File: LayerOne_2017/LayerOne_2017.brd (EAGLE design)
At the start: 73.6 x 73.7 mm, 71 parts, among them IC1 STM32F446_LQFP64LQFP64, IC2 REG1117, J1 SPI_TFT_DISPLAY, Q1 2N2222, Q2 MMBT2222A, U1 SN65HVD235DR, U2 SN65HVD235DR, U4 SDCARD, U5 FERRITE0805, X1 STEREOJACK, X2 MINI-USB-32005-301

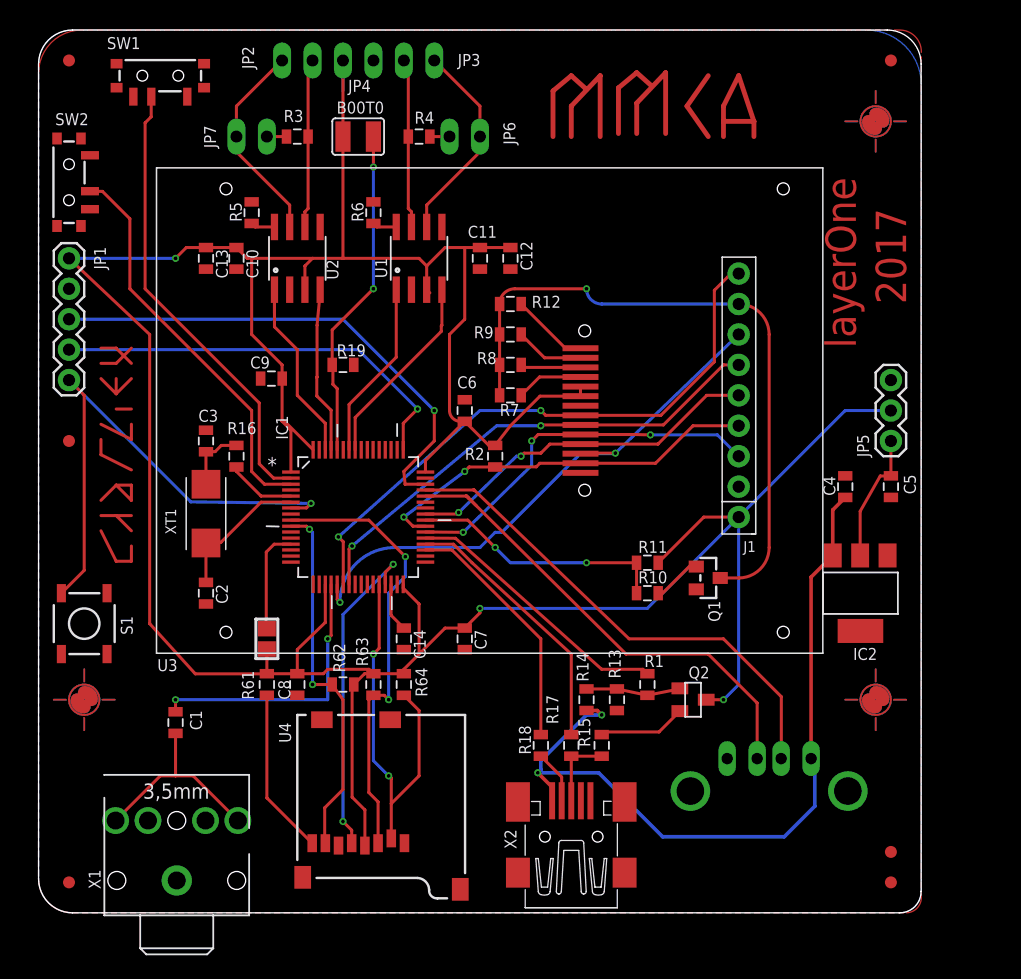
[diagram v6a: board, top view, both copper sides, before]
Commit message: updates to smaller lqfp64 board.
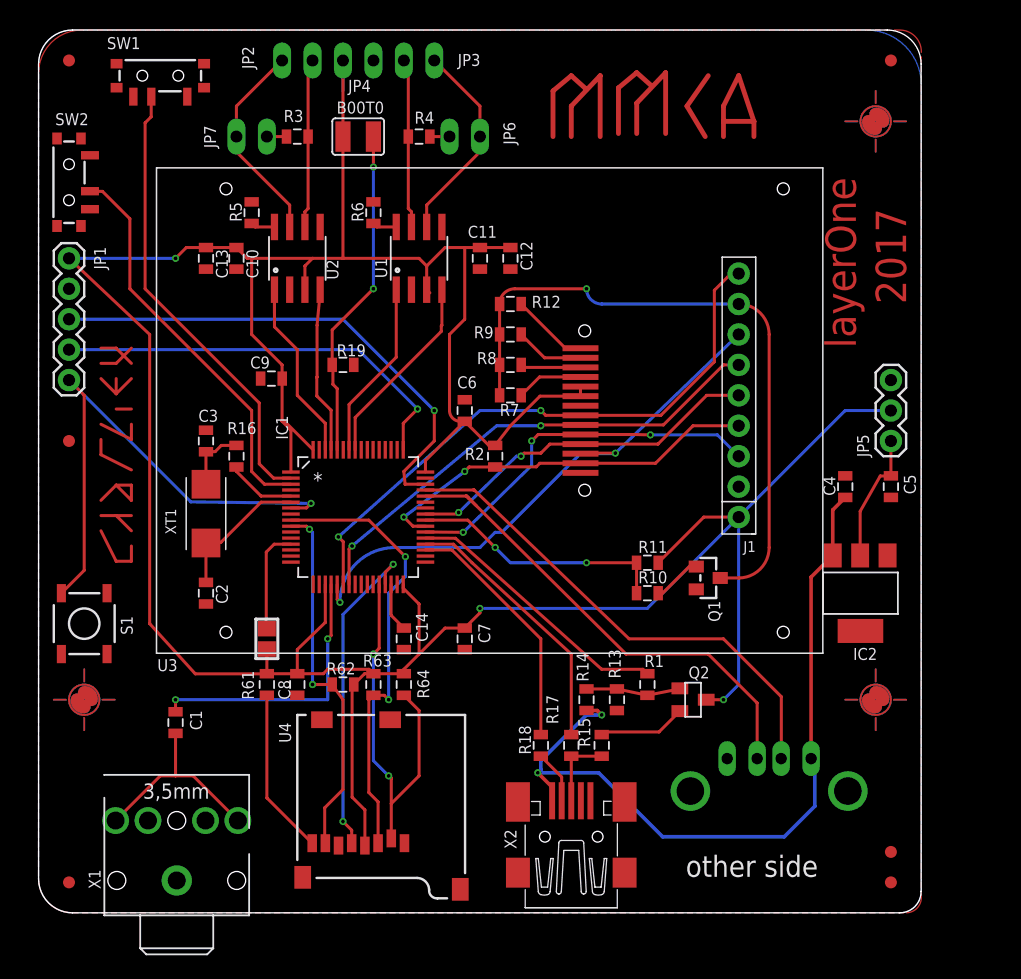
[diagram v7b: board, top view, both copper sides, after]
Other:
- board text added: "other side"
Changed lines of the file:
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@@
 <setting verticaltext="up"/>
 </settings>
-<grid distance="0.05" unitdist="inch" unit="mm" style="lines" multiple="1" display="yes" altdistance="0.001" altunitdist="inch" altunit="inch"/>
+<grid distance="0.05" unitdist="inch" unit="inch" style="lines" multiple="1" display="yes" altdistance="0.005" altunitdist="inch" altunit="inch"/>
 <layers>
 <layer number="1" name="Top" color="4" fill="1" visible="yes" active="yes"/>
@@
 <layer number="14" name="Route14" color="1" fill="6" visible="no" active="no"/>
 <layer number="15" name="Route15" color="4" fill="6" visible="no" active="no"/>
-<layer number="16" name="Bottom" color="1" fill="1" visible="no" active="yes"/>
+<layer number="16" name="Bottom" color="1" fill="1" visible="yes" active="yes"/>
 <layer number="17" name="Pads" color="2" fill="1" visible="yes" active="yes"/>
 <layer number="18" name="Vias" color="2" fill="1" visible="yes" active="yes"/>
@@
 <layer number="49" name="Reference" color="7" fill="1" visible="no" active="yes"/>
 <layer number="50" name="dxf" color="7" fill="1" visible="no" active="no"/>
-<layer number="51" name="tDocu" color="7" fill="1" visible="yes" active="yes"/>
+<layer number="51" name="tDocu" color="7" fill="1" visible="no" active="yes"/>
 <layer number="52" name="bDocu" color="7" fill="1" visible="no" active="yes"/>
 <layer number="53" name="tGND_GNDA" color="7" fill="9" visible="no" active="no"/>
@@
 <layer number="119" name="KAP_TEKEN" color="7" fill="1" visible="no" active="yes"/>
 <layer number="120" name="120" color="7" fill="1" visible="no" active="yes"/>
-<layer number="121" name="_tsilk" color="7" fill="1" visible="no" active="yes"/>
+<layer number="121" name="_tsilk" color="7" fill="1" visible="yes" active="yes"/>
 <layer number="122" name="_bsilk" color="7" fill="1" visible="no" active="yes"/>
 <layer number="123" name="tTestmark" color="7" fill="1" visible="no" active="yes"/>
@@
 <text x="68.199" y="47.117" size="2.54" layer="1" font="vector" rot="R90">layerOne</text>
 <text x="72.39" y="50.8" size="2.54" layer="1" font="vector" rot="R90">2017</text>
+<text x="54" y="3" size="1.778" layer="121">other side</text>
 </plain>
 <attributes>
@@
 <attribute name="DIGIKEY" value="RMCF0603JT10K0CT-ND" x="-87.63" y="100.33" size="1.778" layer="27" display="off"/>
 <attribute name="OC_NEWARK" value="unknown" x="-87.63" y="100.33" size="1.778" layer="27" display="off"/>
-<attribute name="NAME" x="25.5905" y="20.066" size="1" layer="25" ratio="10" rot="R90"/>
+<attribute name="NAME" x="26.4414" y="20.8915" size="1" layer="25" ratio="10" rot="R180"/>
 <attribute name="VALUE" x="24.384" y="17.653" size="0.4064" layer="27"/>
 </element>
@@
 <attribute name="DIGIKEY" value="RMCF0603JT10K0CT-ND" x="-60.96" y="-12.7" size="1.778" layer="27" rot="R90" display="off"/>
 <attribute name="OC_NEWARK" value="unknown" x="-60.96" y="-12.7" size="1.778" layer="27" rot="R90" display="off"/>
-<attribute name="NAME" x="27.4955" y="20.574" size="1" layer="25" ratio="10" rot="R90"/>
+<attribute name="NAME" x="29.4894" y="21.5519" size="1" layer="25" ratio="10" rot="R180"/>
 <attribute name="VALUE" x="29.337" y="18.034" size="0.4064" layer="27" rot="R90"/>
 </element>
@@
 <attribute name="DIGIKEY" value="RMCF0603JT10K0CT-ND" x="-58.42" y="-22.86" size="1.778" layer="27" rot="R90" display="off"/>
 <attribute name="OC_NEWARK" value="unknown" x="-58.42" y="-22.86" size="1.778" layer="27" rot="R90" display="off"/>
-<attribute name="NAME" x="32.4485" y="18.034" size="1" layer="25" ratio="10" rot="R90"/>
+<attribute name="NAME" x="32.6009" y="17.8816" size="1" layer="25" ratio="10" rot="R90"/>
 <attribute name="VALUE" x="31.877" y="18.034" size="0.4064" layer="27" rot="R90"/>
 </element>
@@
 </element>
 <element name="C7" library="SparkFun-Passives" package="0805" value="100nF" x="35.56" y="22.86" smashed="yes" rot="R270">
-<attribute name="NAME" x="36.3855" y="23.622" size="1" layer="25" ratio="10" rot="R270"/>
+<attribute name="NAME" x="36.6903" y="24.1554" size="1" layer="25" ratio="10" rot="R270"/>
 <attribute name="VALUE" x="34.163" y="23.876" size="0.4064" layer="27" rot="R270"/>
 </element>
@@
 </element>
 <element name="C14" library="SparkFun-Passives" package="0805" value="4.7uF/X7R" x="30.48" y="22.86" smashed="yes" rot="R270">
-<attribute name="NAME" x="31.3055" y="23.622" size="1" layer="25" ratio="10" rot="R270"/>
+<attribute name="NAME" x="31.4833" y="25.0444" size="1" layer="25" ratio="10" rot="R270"/>
 <attribute name="VALUE" x="29.083" y="23.876" size="0.4064" layer="27" rot="R270"/>
 </element>
@@
 <vertex x="71.86395" y="0" curve="90"/>
 </polygon>
-<polygon width="0.4064" layer="1" isolate="0.3" orphans="yes">
+<polygon width="0.4064" layer="1" isolate="0.34" orphans="yes">
 <vertex x="73.66" y="1.27"/>
 <vertex x="73.66" y="71.86395" curve="90"/>
@@
 <contactref element="SW2" pad="C"/>
 <contactref element="S1" pad="1"/>
-<wire x1="67.31" y1="36.46" x2="71.12" y2="34.66" width="0" layer="19" extent="1-1"/>
-<wire x1="70.8406" y1="29.8196" x2="71.12" y2="34.66" width="0" layer="19" extent="1-1"/>
-<wire x1="58.42" y1="35.56" x2="67.31" y2="36.46" width="0" layer="19" extent="1-1"/>
-<wire x1="54.88" y1="26.99" x2="58.42" y2="35.56" width="0" layer="19" extent="1-1"/>
-<wire x1="48.26" y1="16.88" x2="54.88" y2="26.99" width="0" layer="19" extent="1-1"/>
-<wire x1="46.05" y1="9.35" x2="48.26" y2="16.88" width="0" layer="19" extent="1-1"/>
-<wire x1="57.46" y1="12.87" x2="48.26" y2="16.88" width="0" layer="19" extent="1-1"/>
-<wire x1="35.19" y1="1.96" x2="46.05" y2="9.35" width="0" layer="19" extent="1-1"/>
-<wire x1="25.03" y1="5.61" x2="35.19" y2="1.96" width="0" layer="19" extent="1-1"/>
-<wire x1="22.04" y1="2.96" x2="25.03" y2="5.61" width="0" layer="19" extent="1-1"/>
-<wire x1="11.53" y1="2.7" x2="22.04" y2="2.96" width="0" layer="19" extent="1-1"/>
-<wire x1="23.64" y1="16.11" x2="25.03" y2="5.61" width="0" layer="19" extent="1-1"/>
-<wire x1="21.59" y1="18.15" x2="23.64" y2="16.11" width="0" layer="19" extent="1-1"/>
-<wire x1="29.34" y1="16.11" x2="23.64" y2="16.11" width="0" layer="19" extent="1-1"/>
-<wire x1="30.48" y1="21.96" x2="29.34" y2="16.11" width="0" layer="19" extent="1-1"/>
-<wire x1="35.56" y1="21.96" x2="30.48" y2="21.96" width="0" layer="19" extent="1-1"/>
+<wire x1="35.56" y1="42.81" x2="32.2834" y2="36.2712" width="0" layer="19" extent="1-1"/>
+<wire x1="20.955" y1="51.9938" x2="16.51" y2="53.71" width="0" layer="19" extent="1-1"/>
+<wire x1="30.48" y1="21.96" x2="35.56" y2="21.96" width="0" layer="19" extent="1-1"/>
 <wire x1="29.9212" y1="27.4066" x2="30.48" y2="21.96" width="0" layer="19" extent="1-1"/>
+<wire x1="29.34" y1="16.11" x2="30.48" y2="21.96" width="0" layer="19" extent="1-1"/>
+<wire x1="23.64" y1="16.11" x2="29.34" y2="16.11" width="0" layer="19" extent="1-1"/>
+<wire x1="31.115" y1="51.9938" x2="36.83" y2="53.71" width="0" layer="19" extent="1-1"/>
 <wire x1="23.4188" y1="27.4066" x2="29.9212" y2="27.4066" width="0" layer="19" extent="1-1"/>
 <wire x1="21.0566" y1="31.2674" x2="23.4188" y2="27.4066" width="0" layer="19" extent="1-1"/>
-<wire x1="23.4188" y1="38.6334" x2="21.0566" y2="31.2674" width="0" layer="19" extent="1-1"/>
-<wire x1="26.3" y1="45.72" x2="23.4188" y2="38.6334" width="0" layer="19" extent="1-1"/>
-<wire x1="18.531" y1="44.577" x2="23.4188" y2="38.6334" width="0" layer="19" extent="1-1"/>
-<wire x1="13.97" y1="40.27" x2="18.531" y2="44.577" width="0" layer="19" extent="1-1"/>
-<wire x1="20.955" y1="51.9938" x2="18.531" y2="44.577" width="0" layer="19" extent="1-1"/>
-<wire x1="16.51" y1="53.71" x2="20.955" y2="51.9938" width="0" layer="19" extent="1-1"/>
-<wire x1="13.97" y1="53.71" x2="16.51" y2="53.71" width="0" layer="19" extent="1-1"/>
-<wire x1="17.78" y1="59.32" x2="16.51" y2="53.71" width="0" layer="19" extent="1-1"/>
-<wire x1="31.115" y1="51.9938" x2="26.3" y2="45.72" width="0" layer="19" extent="1-1"/>
-<wire x1="36.83" y1="53.71" x2="31.115" y2="51.9938" width="0" layer="19" extent="1-1"/>
-<wire x1="39.37" y1="53.71" x2="36.83" y2="53.71" width="0" layer="19" extent="1-1"/>
-<wire x1="27.94" y1="59.32" x2="31.115" y2="51.9938" width="0" layer="19" extent="1-1"/>
-<wire x1="13.97" y1="25.77" x2="21.0566" y2="31.2674" width="0" layer="19" extent="1-1"/>
-<wire x1="5.715" y1="26.67" x2="13.97" y2="25.77" width="0" layer="19" extent="1-1"/>
-<wire x1="32.2834" y1="36.2712" x2="29.9212" y2="27.4066" width="0" layer="19" extent="1-1"/>
-<wire x1="35.56" y1="42.81" x2="32.2834" y2="36.2712" width="0" layer="19" extent="1-1"/>
-<wire x1="45.22" y1="42.31" x2="35.56" y2="42.81" width="0" layer="19" extent="1-1"/>
-<wire x1="45.22" y1="36.71" x2="45.22" y2="42.31" width="0" layer="19" extent="1-1"/>
-<wire x1="4.29" y1="58.71" x2="13.97" y2="53.71" width="0" layer="19" extent="1-1"/>
-<wire x1="2.54" y1="52.07" x2="4.29" y2="58.71" width="0" layer="19" extent="1-1"/>
-<wire x1="7.91" y1="68.1" x2="4.29" y2="58.71" width="0" layer="19" extent="1-1"/>
-<wire x1="27.94" y1="71.12" x2="27.94" y2="59.32" width="0" layer="19" extent="1-1"/>
+<wire x1="23.4188" y1="38.6334" x2="26.3" y2="45.72" width="0" layer="19" extent="1-1"/>
+<wire x1="48.26" y1="16.88" x2="46.05" y2="9.35" width="0" layer="19" extent="1-1"/>
 </signal>
 <signal name="SD_MOSI">
@@
 <signal name="N$27">
 <wire x1="55.88" y1="69.85" x2="54.102" y2="67.31" width="0.4064" layer="1"/>
-<wire x1="54.102" y1="67.31" x2="55.88" y2="64.77" width="0.4064" layer="1"/>
+<wire x1="54.102" y1="67.31" x2="55.626" y2="64.77" width="0.4064" layer="1"/>
 </signal>
 <signal name="N$28">

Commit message: second pcb
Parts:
- R12, R7, R8, R9: value 10 -> 10R
- moved U$8 8.13 mm to (64.8, 66.0)
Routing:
- net +3V3: track 285.3 -> 283.6 mm
- net D-: track 40.8 -> 40.2 mm
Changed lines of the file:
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@@
 <layer number="23" name="tOrigins" color="15" fill="1" visible="yes" active="yes"/>
 <layer number="24" name="bOrigins" color="15" fill="1" visible="yes" active="yes"/>
-<layer number="25" name="tNames" color="7" fill="1" visible="no" active="yes"/>
+<layer number="25" name="tNames" color="7" fill="1" visible="yes" active="yes"/>
 <layer number="26" name="bNames" color="7" fill="1" visible="no" active="yes"/>
 <layer number="27" name="tValues" color="7" fill="1" visible="no" active="yes"/>
@@
 <layer number="49" name="Reference" color="7" fill="1" visible="no" active="yes"/>
 <layer number="50" name="dxf" color="7" fill="1" visible="no" active="no"/>
-<layer number="51" name="tDocu" color="7" fill="1" visible="no" active="yes"/>
+<layer number="51" name="tDocu" color="7" fill="1" visible="yes" active="yes"/>
 <layer number="52" name="bDocu" color="7" fill="1" visible="no" active="yes"/>
 <layer number="53" name="tGND_GNDA" color="7" fill="9" visible="no" active="no"/>
@@
 <attribute name="VALUE" x="29.337" y="57.404" size="0.4064" layer="27" rot="R90"/>
 </element>
-<element name="R7" library="SparkFun-Passives" package="0805" value="10" x="39.37" y="43.18" smashed="yes">
+<element name="R7" library="SparkFun-Passives" package="0805" value="10R" x="39.37" y="43.18" smashed="yes">
 <attribute name="NAME" x="38.481" y="41.4655" size="1" layer="25" ratio="10"/>
 <attribute name="VALUE" x="38.354" y="41.783" size="0.4064" layer="27"/>
 </element>
-<element name="R8" library="SparkFun-Passives" package="0805" value="10" x="39.37" y="45.72" smashed="yes">
+<element name="R8" library="SparkFun-Passives" package="0805" value="10R" x="39.37" y="45.72" smashed="yes">
 <attribute name="NAME" x="36.576" y="45.7835" size="1" layer="25" ratio="10"/>
 <attribute name="VALUE" x="38.354" y="44.323" size="0.4064" layer="27"/>
 </element>
-<element name="R9" library="SparkFun-Passives" package="0805" value="10" x="39.37" y="48.26" smashed="yes">
+<element name="R9" library="SparkFun-Passives" package="0805" value="10R" x="39.37" y="48.26" smashed="yes">
 <attribute name="NAME" x="36.322" y="47.9425" size="1" layer="25" ratio="10"/>
 <attribute name="VALUE" x="38.354" y="46.863" size="0.4064" layer="27"/>
@@
 </element>
 <element name="R10" library="SparkFun-Passives" package="0805" value="100" x="50.8" y="26.67" smashed="yes">
-<attribute name="NAME" x="50.038" y="27.4955" size="1" layer="25" ratio="10"/>
+<attribute name="NAME" x="50.038" y="24.9555" size="1" layer="25" ratio="10"/>
 <attribute name="VALUE" x="49.784" y="25.273" size="0.4064" layer="27"/>
 </element>
@@
 <attribute name="VALUE" x="65.96" y="21.91" size="0.4064" layer="27" ratio="10" rot="R90"/>
 </element>
-<element name="R12" library="SparkFun-Passives" package="0805" value="10" x="39.37" y="50.8" smashed="yes">
+<element name="R12" library="SparkFun-Passives" package="0805" value="10R" x="39.37" y="50.8" smashed="yes">
 <attribute name="NAME" x="41.148" y="50.4825" size="1" layer="25" ratio="10"/>
 <attribute name="VALUE" x="38.354" y="49.403" size="0.4064" layer="27"/>
@@
 <element name="U$5" library="adafruit" package="FIDUCIAL_1MM" value="FIDUCIAL" x="71.12" y="5.08" smashed="yes"/>
 <element name="U$7" library="adafruit" package="FIDUCIAL_1MM" value="FIDUCIAL" x="2.54" y="71.12" smashed="yes"/>
-<element name="U$8" library="adafruit" package="FIDUCIAL_1MM" value="FIDUCIAL" x="71.12" y="71.12" smashed="yes"/>
+<element name="U$8" library="adafruit" package="FIDUCIAL_1MM" value="FIDUCIAL" x="64.77" y="66.04" smashed="yes"/>
 <element name="U$9" library="adafruit" package="FIDUCIAL_1MM" value="FIDUCIAL" x="2.54" y="2.54" smashed="yes"/>
 <element name="C2" library="SparkFun-Passives" package="0805" value="20pF" x="13.97" y="26.67" smashed="yes" rot="R270">
@@
 </element>
 <element name="R1" library="SparkFun-Passives" package="0805" value="100" x="50.8" y="19.05" smashed="yes" rot="R270">
-<attribute name="NAME" x="50.546" y="20.5105" size="1" layer="25" ratio="10"/>
+<attribute name="NAME" x="51.2445" y="15.875" size="1" layer="25" ratio="10" rot="R90"/>
 <attribute name="VALUE" x="49.403" y="20.066" size="0.4064" layer="27" rot="R270"/>
 </element>
 <element name="R13" library="SparkFun-Passives" package="0805" value="36K" x="48.26" y="17.78" smashed="yes" rot="R90">
-<attribute name="NAME" x="48.5775" y="19.558" size="1" layer="25" ratio="10" rot="R90"/>
+<attribute name="NAME" x="48.8315" y="19.558" size="1" layer="25" ratio="10" rot="R90"/>
 <attribute name="VALUE" x="49.657" y="16.764" size="0.4064" layer="27" rot="R90"/>
 </element>
 <element name="R14" library="SparkFun-Passives" package="0805" value="10K" x="45.72" y="17.78" smashed="yes" rot="R270">
-<attribute name="NAME" x="44.8945" y="21.717" size="1" layer="25" ratio="10" rot="R270"/>
+<attribute name="NAME" x="45.2755" y="22.098" size="1" layer="25" ratio="10" rot="R270"/>
 <attribute name="VALUE" x="44.323" y="18.796" size="0.4064" layer="27" rot="R270"/>
 </element>
 <element name="R15" library="SparkFun-Passives" package="0805" value="1K5" x="46.99" y="13.97" smashed="yes" rot="R90">
-<attribute name="NAME" x="46.0375" y="13.843" size="1" layer="25" ratio="10" rot="R90"/>
+<attribute name="NAME" x="48.9585" y="12.192" size="1" layer="25" ratio="10" rot="R90"/>
 <attribute name="VALUE" x="48.387" y="12.954" size="0.4064" layer="27" rot="R90"/>
 </element>
@@
 <attribute name="MPN" value="RMCF0603JT10K0" x="44.45" y="13.97" size="1.778" layer="27" rot="R90" display="off"/>
 <attribute name="PARTNO" value="RMCF0603JT10K0" x="44.45" y="13.97" size="1.778" layer="27" rot="R90" display="off"/>
-<attribute name="NAME" x="43.3705" y="15.748" size="1" layer="25" ratio="10" rot="R90"/>
+<attribute name="NAME" x="44.0055" y="15.621" size="1" layer="25" ratio="10" rot="R90"/>
 <attribute name="VALUE" x="45.847" y="12.954" size="0.4064" layer="27" rot="R90"/>
 </element>
@@
 <wire x1="30.4292" y1="27.4066" x2="30.4292" y2="27.0858" width="0.254" layer="1"/>
 <wire x1="30.4292" y1="27.0858" x2="31.75" y2="25.765" width="0.254" layer="1"/>
-<wire x1="20.32" y1="41.01" x2="20.5342" y2="41.01" width="0.254" layer="1"/>
-<wire x1="20.5342" y1="41.01" x2="22.9108" y2="38.6334" width="0.254" layer="1"/>
-<wire x1="21.0566" y1="36.7792" x2="21.0566" y2="40.2734" width="0.254" layer="1"/>
+<wire x1="21.0566" y1="36.7792" x2="21.0566" y2="38.6334" width="0.254" layer="1"/>
 <wire x1="21.0566" y1="40.2734" x2="20.32" y2="41.01" width="0.254" layer="1"/>
+<wire x1="22.9108" y1="38.6334" x2="21.0566" y2="38.6334" width="0.254" layer="1"/>
+<wire x1="21.0566" y1="38.6334" x2="21.0566" y2="40.2734" width="0.254" layer="1"/>
 </signal>
 <signal name="VCC" class="1">
@@
 <contactref element="IC1" pad="44"/>
 <contactref element="CN1" pad="D+"/>
-<wire x1="59.96" y1="12.87" x2="59.96" y2="17.51" width="0.254" layer="1"/>
-<wire x1="59.96" y1="17.51" x2="55.88" y2="21.59" width="0.254" layer="1"/>
-<wire x1="55.88" y1="21.59" x2="49.022" y2="21.59" width="0.254" layer="1"/>
-<wire x1="49.022" y1="21.59" x2="35.87688125" y2="34.609928125" width="0.254" layer="1"/>
-<wire x1="35.87688125" y1="34.609928125" x2="35.687" y2="34.798" width="0.254" layer="1"/>
-<wire x1="35.714209375" y1="34.7726" x2="35.87688125" y2="34.609928125" width="0.254" layer="1"/>
 <wire x1="32.2834" y1="34.7726" x2="35.7203125" y2="34.7726" width="0.254" layer="1"/>
-<wire x1="35.7203125" y1="34.7726" x2="36.51795625" y2="33.97495625" width="0.254" layer="1"/>
-<wire x1="35.7203125" y1="34.7726" x2="35.714209375" y2="34.7726" width="0" layer="19" extent="1-1"/>
+<wire x1="35.7203125" y1="34.7726" x2="48.9029125" y2="21.59" width="0.254" layer="1"/>
+<wire x1="48.9029125" y1="21.59" x2="57.15" y2="21.59" width="0.254" layer="1"/>
+<wire x1="57.15" y1="21.59" x2="59.96" y2="18.78" width="0.254" layer="1"/>
+<wire x1="59.96" y1="18.78" x2="59.96" y2="12.87" width="0.254" layer="1"/>
 </signal>
 <signal name="D+">
@@
 <wire x1="61.976" y1="12.886" x2="61.96" y2="12.87" width="0.254" layer="1"/>
 <wire x1="61.976" y1="18.034" x2="57.15" y2="22.86" width="0.254" layer="1"/>
-<wire x1="57.15" y1="22.86" x2="49.276" y2="22.86" width="0.254" layer="1"/>
-<wire x1="49.276" y1="22.86" x2="36.322" y2="35.306" width="0.254" layer="1"/>
+<wire x1="57.15" y1="22.86" x2="48.7172" y2="22.86" width="0.254" layer="1"/>
 <wire x1="32.2834" y1="35.2806" x2="36.2966" y2="35.2806" width="0.254" layer="1"/>
-<wire x1="36.2966" y1="35.2806" x2="36.322" y2="35.306" width="0.254" layer="1"/>
+<wire x1="36.2966" y1="35.2806" x2="48.7172" y2="22.86" width="0.254" layer="1"/>
 </signal>
 <signal name="AUDIO_OUT">
